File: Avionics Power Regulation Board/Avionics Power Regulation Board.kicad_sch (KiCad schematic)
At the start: 17 parts, among them U1 LM2576HVS-5, U4 TPS61085DGK

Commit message: Updated Subscale Board
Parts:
- R1, R2, Rcomp1: footprint MFR_25FRF52_10K:RESAD1100W55L680D260 -> Resistor_SMD:R_0805_2012Metric_Pad1.20x1.40mm_HandSolder
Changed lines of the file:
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@@
 			)
 		)
-		(property "Footprint" "MFR_25FRF52_10K:RESAD1100W55L680D260"
+		(property "Footprint" "Resistor_SMD:R_0805_2012Metric_Pad1.20x1.40mm_HandSolder"
 			(at 91.186 80.264 90)
 			(effects
@@
 			)
 		)
-		(property "Footprint" "MFR_25FRF52_10K:RESAD1100W55L680D260"
+		(property "Footprint" "Resistor_SMD:R_0805_2012Metric_Pad1.20x1.40mm_HandSolder"
 			(at 78.486 92.964 90)
 			(effects
@@
 			)
 		)
-		(property "Footprint" "MFR_25FRF52_10K:RESAD1100W55L680D260"
+		(property "Footprint" "Resistor_SMD:R_0805_2012Metric_Pad1.20x1.40mm_HandSolder"
 			(at 91.186 90.424 90)
 			(effects

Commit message: Completely Redone
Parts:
- added H1, H2: MountingHole, MountingHole:MountingHole_2.1mm, symbol Mechanical:MountingHole
- added J1: Conn_01x05_Socket, Connector_PinHeader_2.54mm:PinHeader_1x05_P2.54mm_Vertical, symbol Connector:Conn_01x05_Pin
- C2: footprint Capacitor_THT:C_Radial_D5.0mm_H11.0mm_P2.00mm -> Capacitor_THT:C_Radial_D10.0mm_H16.0mm_P5.00mm
- L1: footprint RLB9012-101KL:IND_RLB9012-101KL -> Inductor_THT:L_Radial_D6.0mm_P4.00mm
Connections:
- net GNDREF: now also J1.1 (Pin_1)
- net VOUT: now also J1.2 (Pin_2)
- new net ALERT: J1.5 (Pin_5)
- new net SCL: J1.4 (Pin_4)
- new net SDA: J1.3 (Pin_3)
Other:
- removed sheet Pi Pico and Instruments
- note added: "Mounting Holes"
- note added: "OUTPUT PINS"

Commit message: Fixed
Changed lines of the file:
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@@
+	(wire
+		(pts
+			(xy 67.31 39.37) (xy 67.31 40.64)
+		)
+		(stroke
+			(width 0)
+			(type default)
+		)
+	)
 	(wire
 		(pts
@@
 	(symbol
 		(lib_id "power:GNDREF")
-		(at 67.31 39.37 0)
-		(unit 1)
-		(exclude_from_sim no)
-		(in_bom yes)
-		(on_board yes)
-		(dnp no)
-		(fields_autoplaced yes)
-		(property "Reference" "#PWR03"
-			(at 67.31 45.72 0)
-			(effects
-				(font
-					(size 1.27 1.27)
-				)
-				(hide yes)
-			)
-		)
-		(property "Value" "GNDREF"
-			(at 67.31 44.45 0)
-			(effects
-				(font
-					(size 1.27 1.27)
-				)
-			)
-		)
-		(property "Footprint" ""
-			(at 67.31 39.37 0)
-			(effects
-				(font
-					(size 1.27 1.27)
-				)
-				(hide yes)
-			)
-		)
-		(property "Datasheet" ""
-			(at 67.31 39.37 0)
-			(effects
-				(font
-					(size 1.27 1.27)
-				)
-				(hide yes)
-			)
-		)
-		(property "Description" "Power symbol creates a global label with name \"GNDREF\" , reference supply ground"
-			(at 67.31 39.37 0)
-			(effects
-				(font
-					(size 1.27 1.27)
-				)
-				(hide yes)
-			)
-		)
-		(pin "1"
-		)
-		(instances
-			(project "Avionics Power Regulation Board"
-				(path "/39b96ce3-0d1f-4af7-8d8c-7f35e443ce2d"
-					(reference "#PWR03")
-					(unit 1)
-				)
-			)
-		)
-	)
-	(symbol
-		(lib_id "power:GNDREF")
 		(at 90.17 96.52 0)
 		(unit 1)
@@
 			)
 		)
+		(property "Purpose" ""
+			(at 60.96 81.28 0)
+			(effects
+				(font
+					(size 1.27 1.27)
+				)
+			)
+		)
+		(property "Sim.Library" "E:\\KiCAD\\Spice Models\\slim133b\\SLIM133A\\TPS61085_PSPICE_TRANS\\tps61085.lib"
+			(at 60.96 81.28 0)
+			(effects
+				(font
+					(size 1.27 1.27)
+				)
+				(hide yes)
+			)
+		)
+		(property "Sim.Name" "TPS61085"
+			(at 60.96 81.28 0)
+			(effects
+				(font
+					(size 1.27 1.27)
+				)
+				(hide yes)
+			)
+		)
+		(property "Sim.Device" "SUBCKT"
+			(at 60.96 81.28 0)
+			(effects
+				(font
+					(size 1.27 1.27)
+				)
+				(hide yes)
+			)
+		)
+		(property "Sim.Pins" "1=EN 2=FB 3=IN 4=SS 5=PGND 6=SW 7=COMP 8=FREQ"
+			(at 60.96 81.28 0)
+			(effects
+				(font
+					(size 1.27 1.27)
+				)
+				(hide yes)
+			)
+		)
 		(pin "8"
 		)
@@
 	)
 	(symbol
+		(lib_id "power:GNDREF")
+		(at 67.31 40.64 0)
+		(unit 1)
+		(exclude_from_sim no)
+		(in_bom yes)
+		(on_board yes)
+		(dnp no)
+		(fields_autoplaced yes)
+		(property "Reference" "#PWR025"
+			(at 67.31 46.99 0)
+			(effects
+				(font
+					(size 1.27 1.27)
+				)
+				(hide yes)
+			)
+		)
+		(property "Value" "GNDREF"
+			(at 67.31 45.72 0)
+			(effects
+				(font
+					(size 1.27 1.27)
+				)
+			)
+		)
+		(property "Footprint" ""
+			(at 67.31 40.64 0)
+			(effects
+				(font
+					(size 1.27 1.27)
+				)
+				(hide yes)
+			)
+		)
+		(property "Datasheet" ""
+			(at 67.31 40.64 0)
+			(effects
+				(font
+					(size 1.27 1.27)
+				)
+				(hide yes)
+			)
+		)
+		(property "Description" "Power symbol creates a global label with name \"GNDREF\" , reference supply ground"
+			(at 67.31 40.64 0)
+			(effects
+				(font
+					(size 1.27 1.27)
+				)
+				(hide yes)
+			)
+		)
+		(pin "1"
+		)
+		(instances
+			(project "Avionics Power Regulation Board"
+				(path "/39b96ce3-0d1f-4af7-8d8c-7f35e443ce2d"
+					(reference "#PWR025")
+					(unit 1)
+				)
+			)
+		)
+	)
+	(symbol
 		(lib_id "Regulator_Switching:LM2576HVS-5")
 		(at 48.26 29.21 0)
@@
 			(at 48.26 29.21 0)
 			(effects
+				(font
+					(size 1.27 1.27)
+				)
+				(hide yes)
+			)
+		)
+		(property "Purpose" ""
+			(at 48.26 29.21 0)
+			(effects
+				(font
+					(size 1.27 1.27)
+				)
+			)
+		)
+		(property "Sim.Library" "E:\\KiCAD\\Spice Models\\slim133b\\SLIM133A\\TPS61085_PSPICE_TRANS\\TPS61085.DSN"
+			(at 48.26 29.21 0)
+			(effects

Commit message: Step Files
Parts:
- L2: footprint AIAP-01-3R3K-T:INDAD1227W51L914D355 -> 3.3uH:IND_BOURNS_RLB9012
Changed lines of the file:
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@@
 			)
 		)
-		(property "Footprint" "AIAP-01-3R3K-T:INDAD1227W51L914D355"
+		(property "Footprint" "3.3uH:IND_BOURNS_RLB9012"
 			(at 60.96 63.5 0)
 			(effects

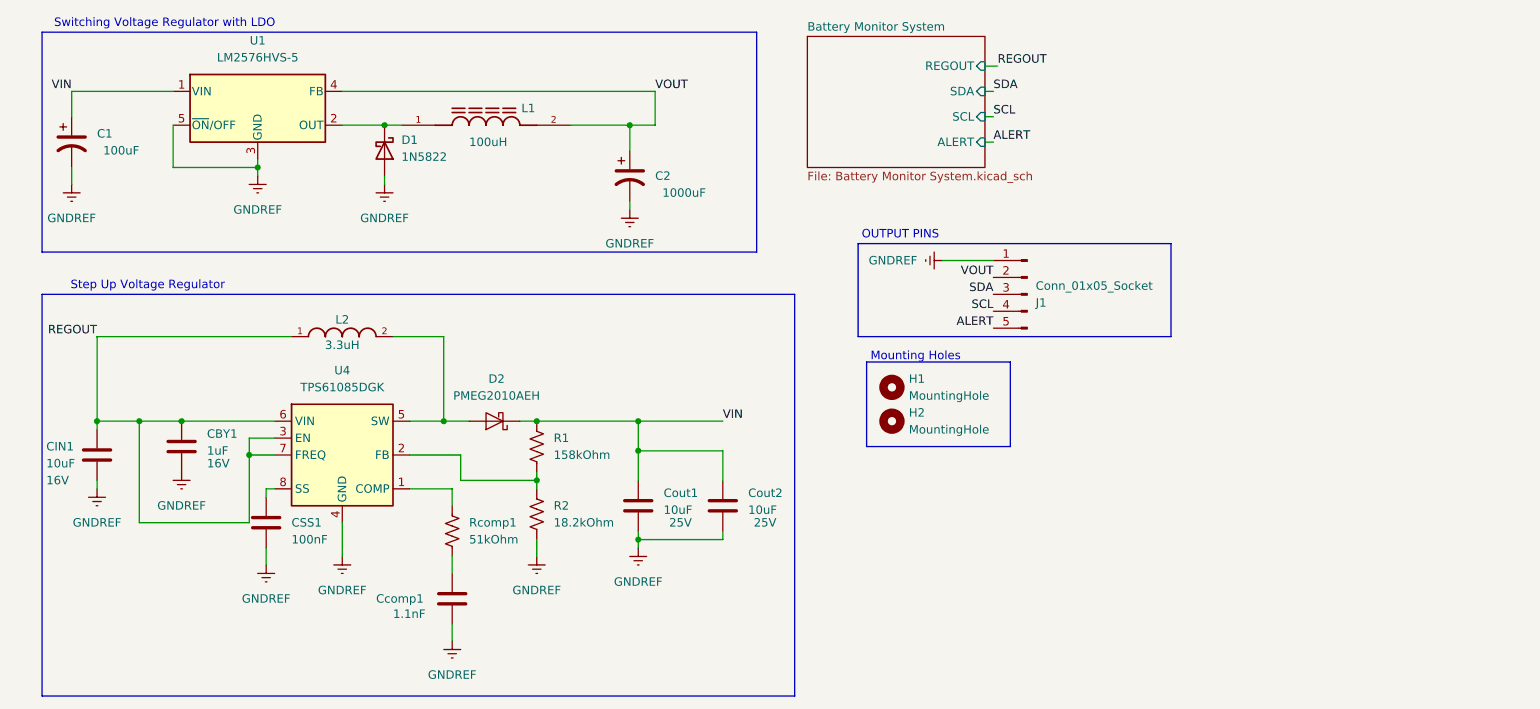
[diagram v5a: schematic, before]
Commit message: Removed one of the transformer
Must Redo the traces when you get home
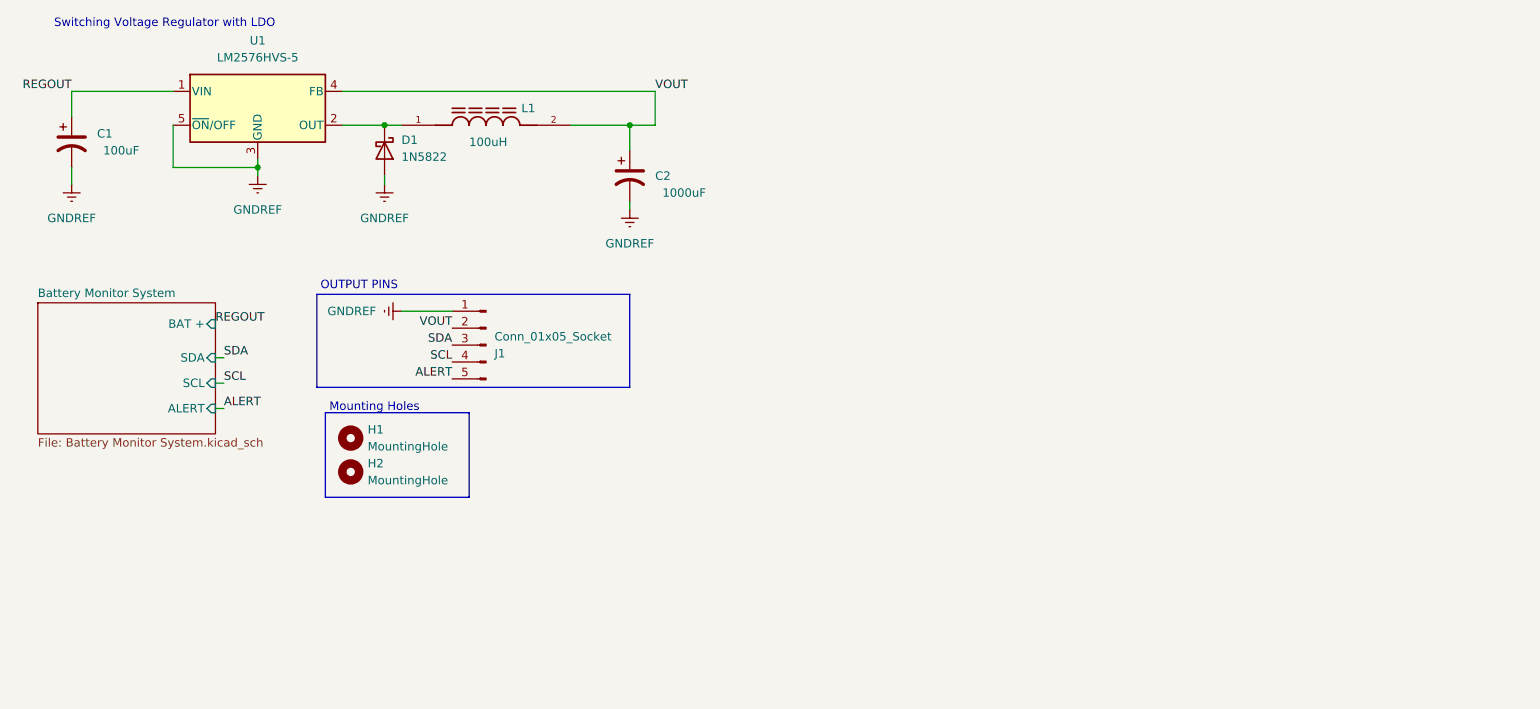
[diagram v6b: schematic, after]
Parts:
- removed CBY1: 1uF, Capacitor_THT:C_Radial_D5.0mm_H11.0mm_P2.00mm, symbol Device:C
- removed CIN1, Cout1, Cout2: 10uF, Capacitor_THT:C_Radial_D4.0mm_H7.0mm_P1.50mm, symbol Device:C
- removed CSS1: 100nF, Capacitor_THT:C_Radial_D4.0mm_H7.0mm_P1.50mm, symbol Device:C
- removed Ccomp1: 1.1nF, Capacitor_THT:C_Disc_D5.1mm_W3.2mm_P5.00mm, symbol Device:C
- removed D2: PMEG2010AEH, Diode_SMD:D_SOD-123F, symbol Diode:PMEG2010AEH
- removed L2: 3.3uH, 3.3uH:IND_BOURNS_RLB9012, symbol DFE252010F-3R3M_P2:DFE252010F-3R3M=P2
- removed R1: 158kOhm, Resistor_SMD:R_0805_2012Metric_Pad1.20x1.40mm_HandSolder, symbol Device:R_US
- removed R2: 18.2kOhm, Resistor_SMD:R_0805_2012Metric_Pad1.20x1.40mm_HandSolder, symbol Device:R_US
- removed Rcomp1: 51kOhm, Resistor_SMD:R_0805_2012Metric_Pad1.20x1.40mm_HandSolder, symbol Device:R_US
- removed U4: TPS61085DGK, Package_SO:VSSOP-8_3x3mm_P0.65mm, symbol Regulator_Switching:TPS61085DGK
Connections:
- net VIN is gone; now on net REGOUT: C1.1, U1.1 (VIN)
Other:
- sheet Battery Monitor System ports: added BAT +; removed REGOUT
- note removed: "Step Up Voltage Regulator"
- moved on the sheet: H1, H2, J1
